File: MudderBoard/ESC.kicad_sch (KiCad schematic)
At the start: 0 parts

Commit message: ESC Schematic
Started ESC Schematic.
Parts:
- added C10: 4.7u, symbol Device:C
- added C11: 0.1u, symbol Device:C_Small
- added C12: 500n, symbol Device:C
- added C13: 470n, symbol Device:C
- added C14: 2.2n, symbol Device:C
- added C15: 47p, symbol Device:C
- added C16: 1u, symbol Device:C
- added R10: R49.9k, symbol Device:R
- added R11: R20.0k, symbol Device:R
- added R12: R10.0k, symbol Device:R
- added R13: R42.2k, symbol Device:R
- added R8: R68.0k, symbol Device:R
- added R9: R6.80k, symbol Device:R
- added U2: ~, LM5123-Q1:LM5123-Q1, symbol LM5123-Q1:LM5123-Q1
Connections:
- new net: C14.1, R13.2
- new net: C11.2, U2.7 (HB)
- new net +BATT: C16.1, R8.1, U2.8 (BIAS)
- new net COMP: C15.1, R13.1, U2.20 (COMP)
- new net GND: C10.2, C12.2, C13.2, C14.2, C15.2, C16.2, R10.2, R12.2, R9.2, U2.10 (PGND), U2.12 (MODE), U2.14 (SYNC/DITHER), U2.19 (AGND)
- new net RT: R10.1, U2.15 (RT)
- new net SS: C12.1, U2.17 (SS)
- new net SW: C11.1, U2.6 (SW)
- new net TRK: R11.2, R12.1, U2.18 (TRK)
- new net UVLO: R8.2, R9.1, U2.13 (UVLO)
- new net VCC: C10.1, U2.9 (VCC)
- new net VREF: C13.1, R11.1, U2.16 (VREF/RANGE)

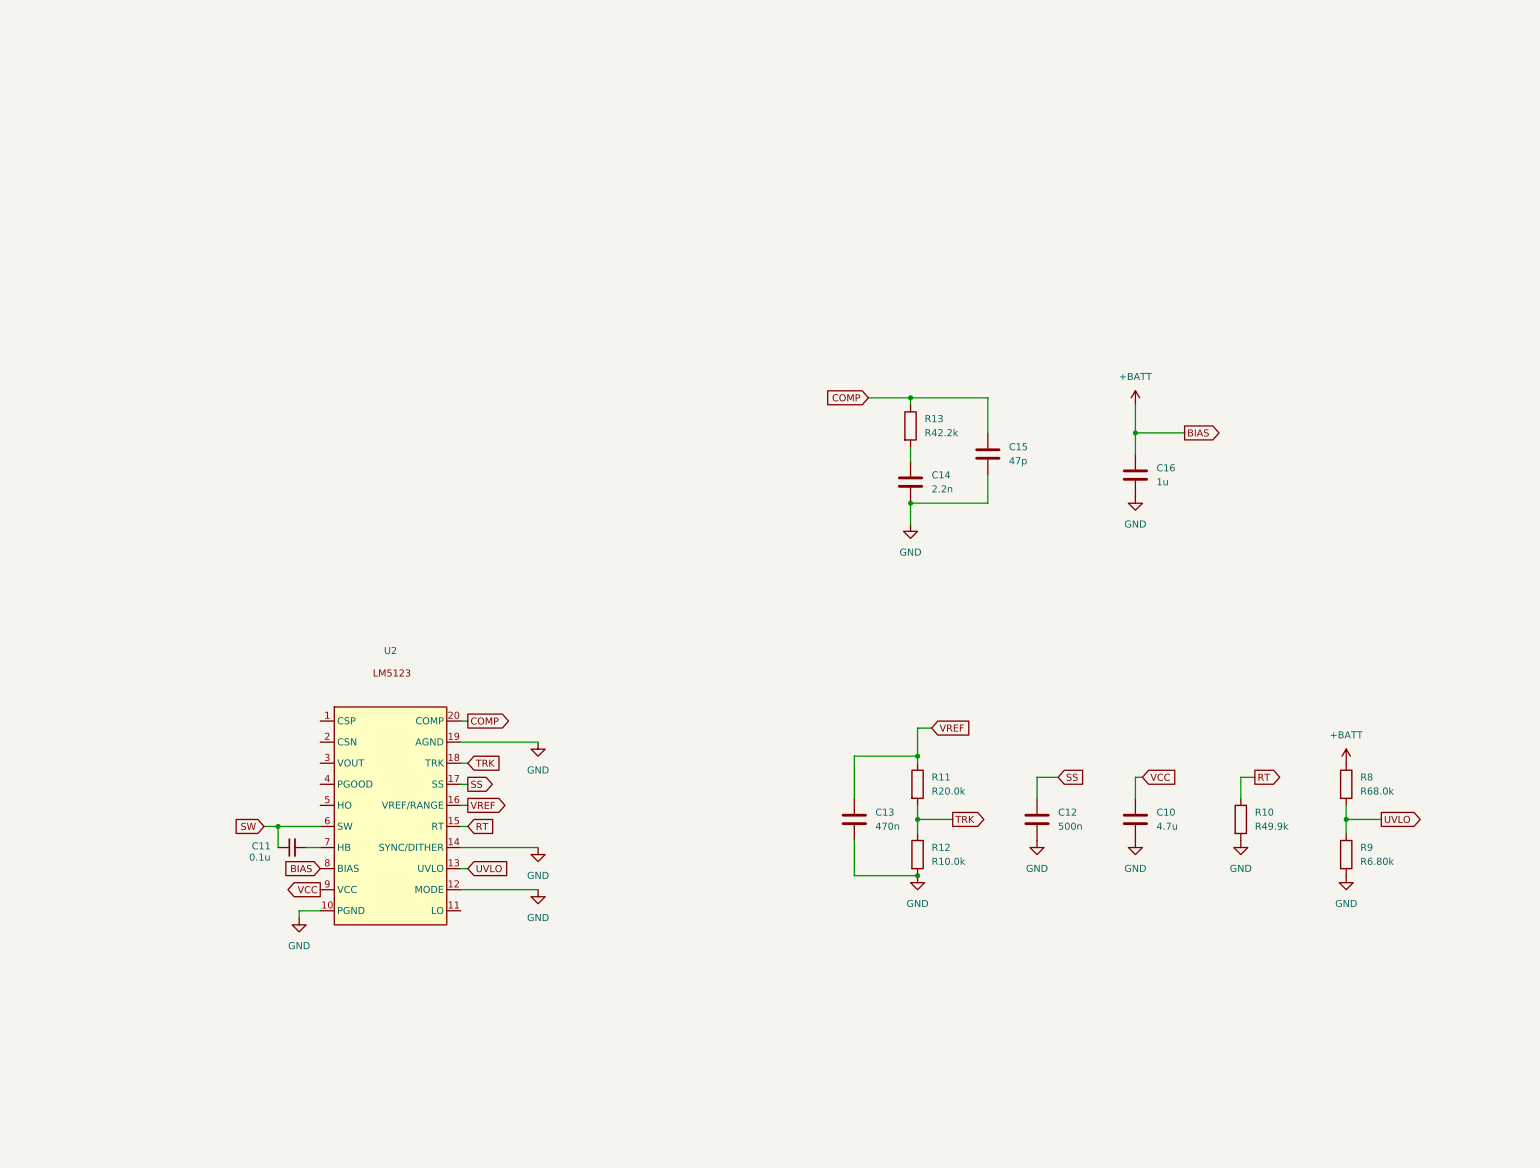
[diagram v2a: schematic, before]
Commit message: Working on ESC Circuit
Still working...
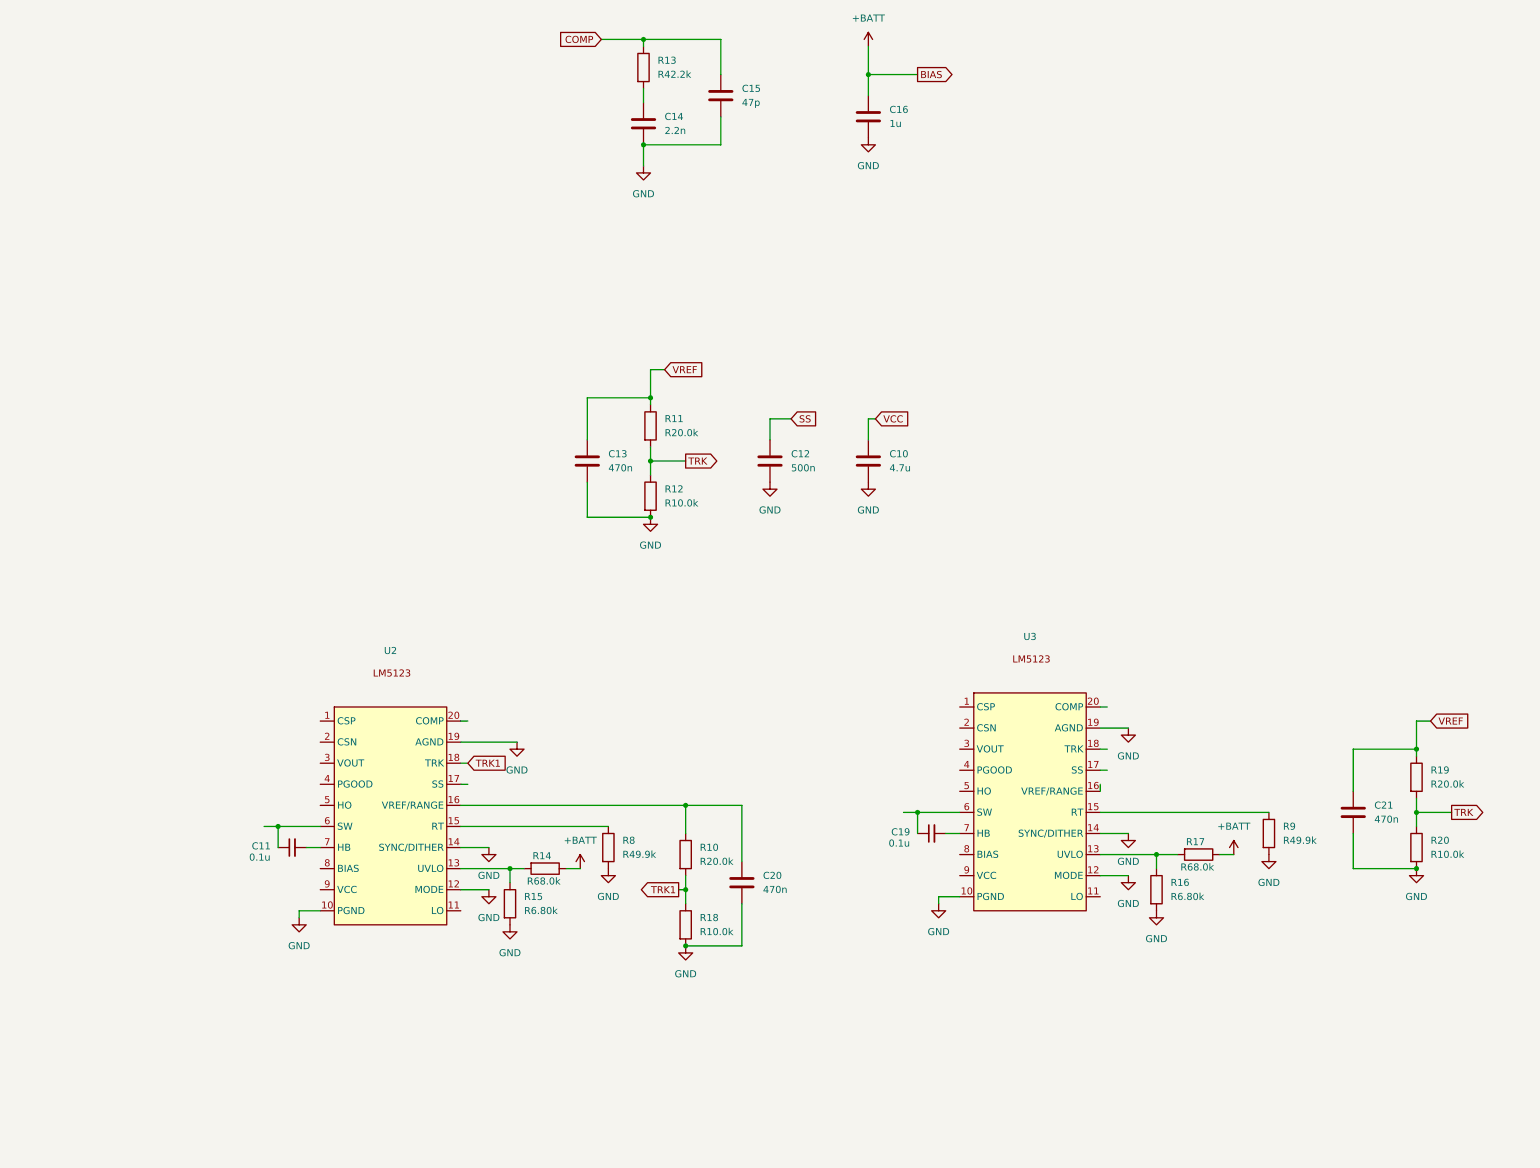
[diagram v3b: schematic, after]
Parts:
- added C19: 0.1u, symbol Device:C_Small
- added C20, C21: 470n, symbol Device:C
- added R14, R17: R68.0k, Resistor_THT:R_Axial_DIN0207_L6.3mm_D2.5mm_P2.54mm_Vertical, symbol Device:R
- added R15, R16: R6.80k, Resistor_THT:R_Axial_DIN0207_L6.3mm_D2.5mm_P2.54mm_Vertical, symbol Device:R
- added R18, R20: R10.0k, Resistor_THT:R_Axial_DIN0207_L6.3mm_D2.5mm_P2.54mm_Vertical, symbol Device:R
- added R19: R20.0k, Resistor_THT:R_Axial_DIN0207_L6.3mm_D2.5mm_P2.54mm_Vertical, symbol Device:R
- added U3: ~, LM5123-Q1:LM5123-Q1, symbol LM5123-Q1:LM5123-Q1
- R10: value R49.9k -> R20.0k; footprint (none) -> Resistor_THT:R_Axial_DIN0207_L6.3mm_D2.5mm_P2.54mm_Vertical
- R11, R12, R13: footprint (none) -> Resistor_THT:R_Axial_DIN0207_L6.3mm_D2.5mm_P2.54mm_Vertical
- R8: value R68.0k -> R49.9k; footprint (none) -> Resistor_THT:R_Axial_DIN0207_L6.3mm_D2.5mm_P2.54mm_Vertical
- R9: value R6.80k -> R49.9k; footprint (none) -> Resistor_THT:R_Axial_DIN0207_L6.3mm_D2.5mm_P2.54mm_Vertical
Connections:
- net +BATT: now also R14.1, R17.1; no longer R8.1, U2.8 (BIAS)
- net COMP: no longer U2.20 (COMP)
- net GND: now also R8.2, C20.2, C21.2, R15.2, R16.2, R18.2, R20.2, U3.10 (PGND), U3.12 (MODE), U3.14 (SYNC/DITHER), U3.19 (AGND); no longer R10.2
- net SS: no longer U2.17 (SS)
- net TRK: now also R19.2, R20.1; no longer U2.18 (TRK)
- net VCC: no longer U2.9 (VCC)
- net VREF: now also C21.1, R19.1; no longer U2.16 (VREF/RANGE)
- net RT: no longer names the net of R10.1
- net RT: now also U2.16 (VREF/RANGE), C20.1; no longer U2.15 (RT)
- net SW: no longer names the net of C11.1, U2.6 (SW)
- removed net UVLO: R8.2, R9.1, U2.13 (UVLO)
- new net: R9.1, U3.15 (RT)
- new net: R14.2, R15.1, U2.13 (UVLO)
- new net: R8.1, U2.15 (RT)
- new net: R16.1, R17.2, U3.13 (UVLO)
- new net: C19.1, U3.6 (SW)
- new net: C19.2, U3.7 (HB)
- new net TRK1: R10.2, R18.1, U2.18 (TRK)
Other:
- moved on the sheet: C10, C12, C13, C14, C15, C16, R11, R12, R13

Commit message: ESC Boost Converter Circuit
Finished design of ESC boost converter design and added some component libraries.
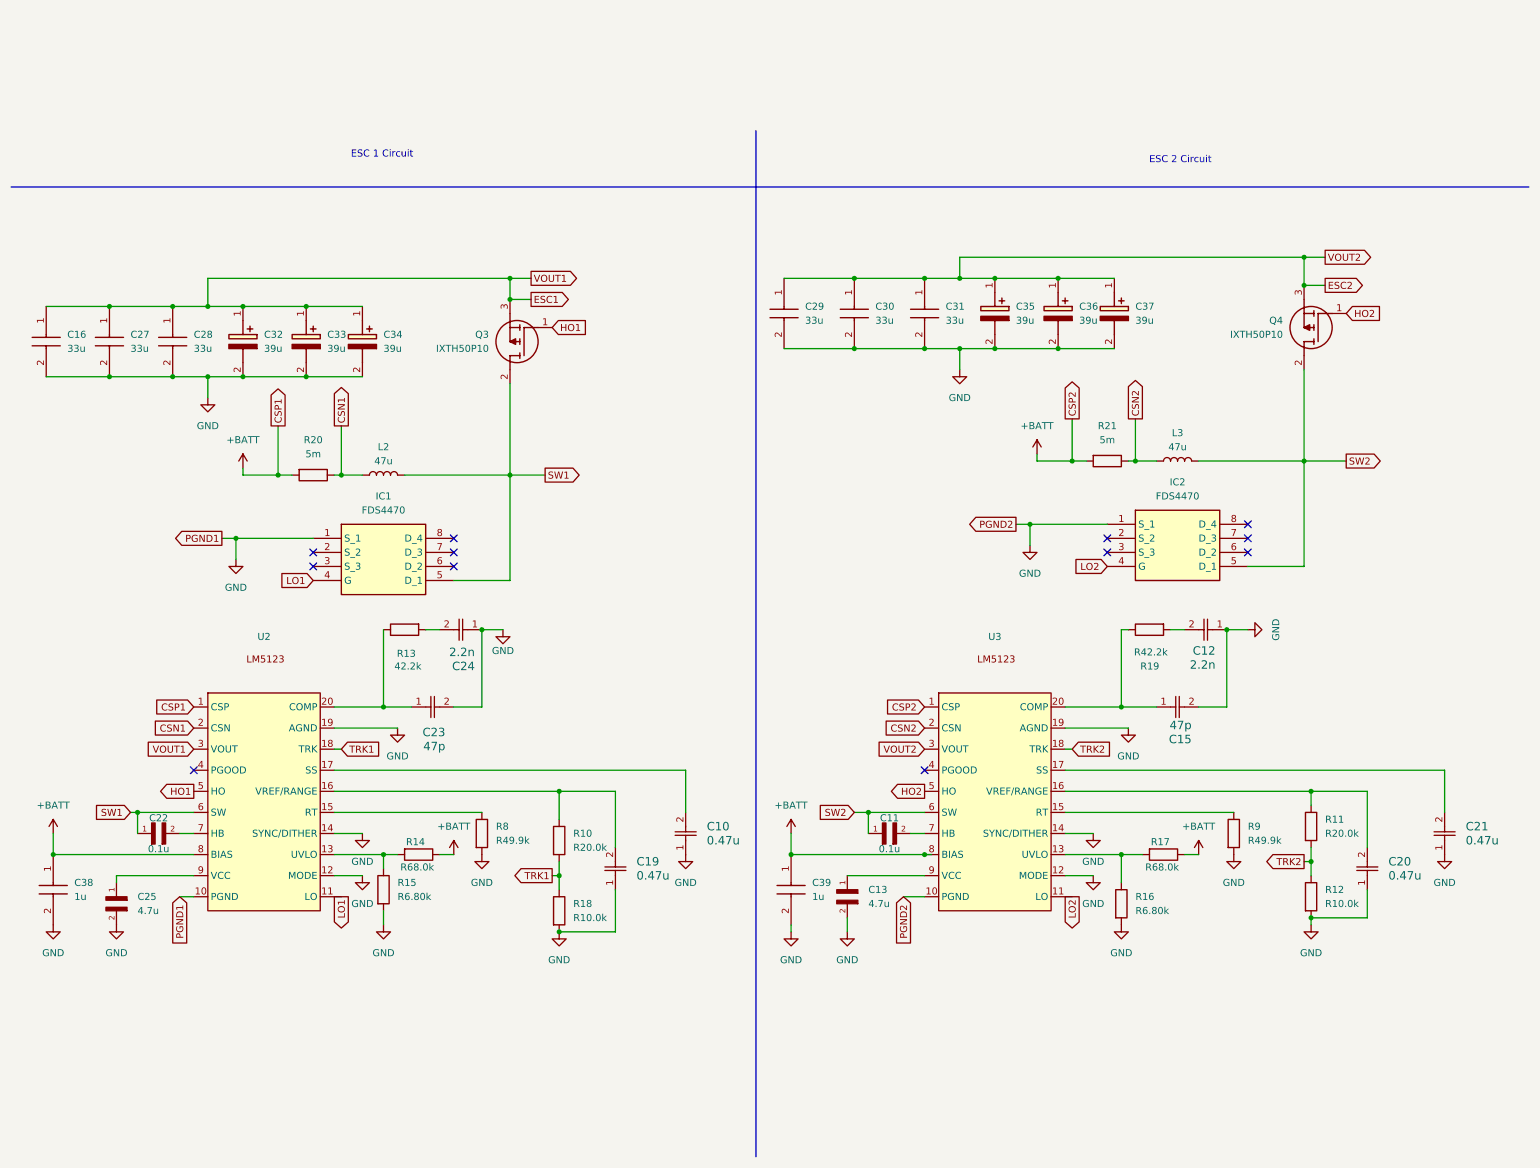
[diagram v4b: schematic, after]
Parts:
- removed C10: 4.7u, symbol Device:C
- removed C11, C19: 0.1u, symbol Device:C_Small
- removed C12: 500n, symbol Device:C
- removed C13, C20, C21: 470n, symbol Device:C
- removed C14: 2.2n, symbol Device:C
- removed C15: 47p, symbol Device:C
- removed C16: 1u, symbol Device:C
- added C10, C19, C20, C21: 0.47u, CAP_1005_TDK, symbol 2024-04-21_19-07-56:CGA2B1X7S1C474K050BC
- added C11, C22: 0.1u, GRM155R71C104KA88J:CAPC1005X55N, symbol GRM155R71C104KA88J:GRM155R71C104KA88J
- added C12, C24: 2.2n, CAP_885012005_WRE, symbol 2024-04-21_19-19-09:885012005029
- added C13, C25: 4.7u, CL10A475KO8NNNC:CAPC1608X90N, symbol CL10A475KO8NNNC:CL10A475KO8NNNC
- added C15, C23: 47p, CAP_885012005_WRE, symbol 2024-04-21_19-19-09:885012005029
- added C16, C27, C28, C29, C30, C31: 33u, FG26, symbol FG26X5R1E336MRT06:FG26X5R1E336MRT06
- added C32, C33, C34, C35, C36, C37: 39u, CAPPRD200W55D500H1200, symbol EEU-FC1E390:EEU-FC1E390
- added C38, C39: 1u, FG20, symbol FG20X7R1C226MRT06:FG20X7R1C226MRT06
- added IC1, IC2: FDS4470, SOIC127P600X175-8N, symbol FDS4470:FDS4470
- added L2, L3: 47u, 2309-V-RC:2309-V-RC, symbol Device:L
- added Q3, Q4: IXTH50P10, TO546P530X1600X2596-3P, symbol IXTH50P10:IXTH50P10
- added R21: 5m, symbol Device:R
- R13: value R42.2k -> 42.2k
- R19: value R20.0k -> R42.2k
- R20: value R10.0k -> 5m; footprint Resistor_THT:R_Axial_DIN0207_L6.3mm_D2.5mm_P2.54mm_Vertical -> (none)
- U2, U3: footprint LM5123-Q1:LM5123-Q1 -> LM5123-Q1:LM5123QRGRRQ1
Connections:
- net COMP is gone; now on an unnamed net: R13.1
- net +BATT: now also R20.2, U2.1 (CSP), U2.8 (BIAS), U3.1 (CSP), U3.8 (BIAS), C38.1, C39.1, R21.2
- net GND: now also C10.1, C12.1, C13.2, C15.2, C16.2, C19.1, C20.1, C21.1, C23.2, C24.1, C25.2, C27.2, C28.2, C29.2, C30.2, C31.2, C32.2 (-), C33.2 (-), C34.2 (-), C35.2 (-), C36.2 (-), C37.2 (-), C38.2, C39.2, IC1.1 (S_1), IC2.1 (S_1); no longer R20.2
- net at R13.2: now also C24.2
- net SW1: now reaches U2.6 (SW)
- net SW1: now also C22.1, IC1.5 (D_1), L2.2, Q3.2 (D)
- net at U2.7 (HB): now also C22.2
- net at R10.1, U2.16 (VREF/RANGE): now also C19.2
- net LO1: now reaches U2.11 (LO)
- net LO1: now also IC1.4 (G)
- net at U2.17 (SS): now also C10.2
- net CSN1: now reaches U2.2 (CSN)
- net CSN1: now also R20.1, L2.1
- net at U2.20 (COMP): now also C23.1
- net ESC1: now reaches U2.3 (VOUT)
- net ESC1: now also C16.1, C27.1, C28.1, C32.1 (+), C33.1 (+), C34.1 (+), Q3.3 (S)
- net HO1: now reaches U2.5 (HO)
- net HO1: now also Q3.1 (G)
- net at U2.9 (VCC): now also C25.1
- net LO2: now reaches U3.11 (LO)
- net LO2: now also IC2.4 (G)
- net at U3.16 (VREF/RANGE): now also R11.1, C20.2
- net at U3.17 (SS): now also C21.2
- net TRK2: now reaches U3.18 (TRK)
- net TRK2: now also R11.2, R12.1
- net CSN2: now reaches U3.2 (CSN)
- net CSN2: now also L3.1, R21.1
- net at U3.20 (COMP): now also R19.1, C15.1
- net ESC2: now reaches U3.3 (VOUT)
- net ESC2: now also C29.1, C30.1, C31.1, C35.1 (+), C36.1 (+), C37.1 (+), Q4.3 (S)
- net HO2: now reaches U3.5 (HO)
- net HO2: now also Q4.1 (G)
- net SW2: now reaches U3.6 (SW)
- net SW2: now also C11.1, IC2.5 (D_1), L3.2, Q4.2 (D)
- net at U3.7 (HB): now also C11.2
- net at U3.9 (VCC): now also C13.1
- removed net TRK: R11.2, R12.1, R19.2, R20.1
- removed net VREF: R11.1, R19.1
- new net: C12.2, R19.2
- no-connect marks 0 -> 12
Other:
- note added: "ESC 1 Circuit"
- note added: "ESC 2 Circuit"
- moved on the sheet: R10, R13, R14, R15, R16, R17, R18, R8, R9, U2, U3
